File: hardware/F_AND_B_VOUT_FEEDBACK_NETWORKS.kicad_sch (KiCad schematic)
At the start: 32 parts, among them Q10 NTA7002NT1G, Q11 NTA7002NT1G, Q12 NTA7002NT1G, Q13 NTA7002NT1G, Q14 NTA7002NT1G, Q15 NTA7002NT1G, Q16 NTA7002NT1G, Q7 NTA7002NT1G, Q8 NTA7002NT1G, Q9 NTA7002NT1G

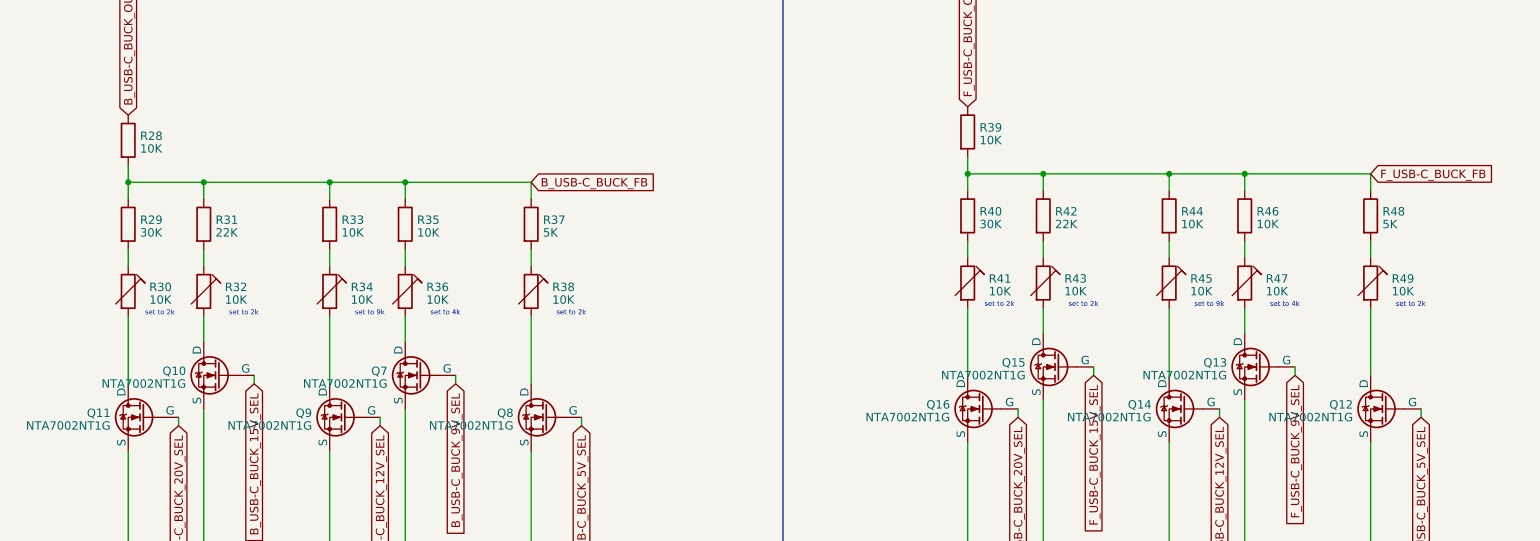
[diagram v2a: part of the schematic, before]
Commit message: migrated to the esp32-s2 and starting new board revison
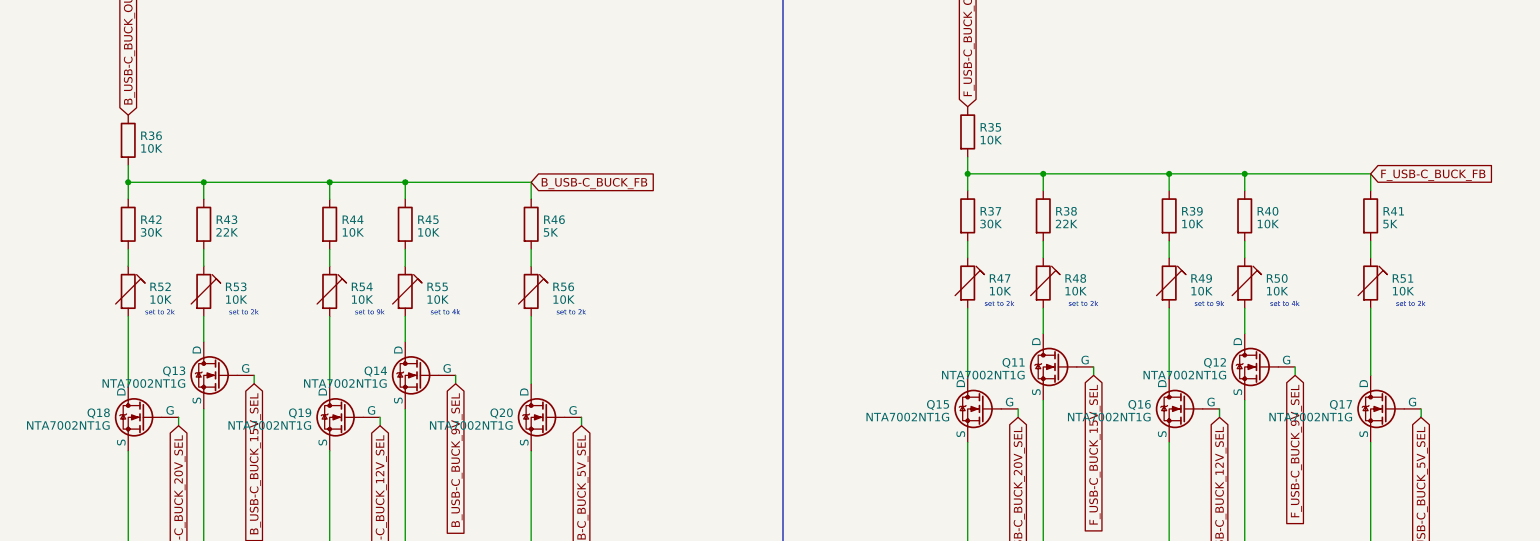
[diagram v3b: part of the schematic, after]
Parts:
- renumbered Q15 to Q11, Q13 to Q12, Q10 to Q13, Q7 to Q14, Q16 to Q15, Q14 to Q16, Q12 to Q17, Q11 to Q18, Q9 to Q19, Q8 to Q20, R39 to R35, R28 to R36, R40 to R37, R42 to R38, R44 to R39, R46 to R40, R48 to R41, R29 to R42, R31 to R43, R33 to R44, R35 to R45, R37 to R46, R41 to R47, R43 to R48, R45 to R49, R47 to R50, R49 to R51, R30 to R52, R32 to R53, R34 to R54, R36 to R55, R38 to R56
